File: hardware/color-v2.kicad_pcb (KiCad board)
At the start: 2 copper layers, 25 x 20 mm, 29 parts, among them P1 CON-SENSOR2, P2 DEBUG, P3 BOOT, Q1 2N7002P, U1 VEML6040, U2 XMC1XXX24, U3 DRILL, U4 DRILL, U5 DRILL, U6 DRILL

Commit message: fix drc error
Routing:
- net GND: track 24.8 -> 26.4 mm

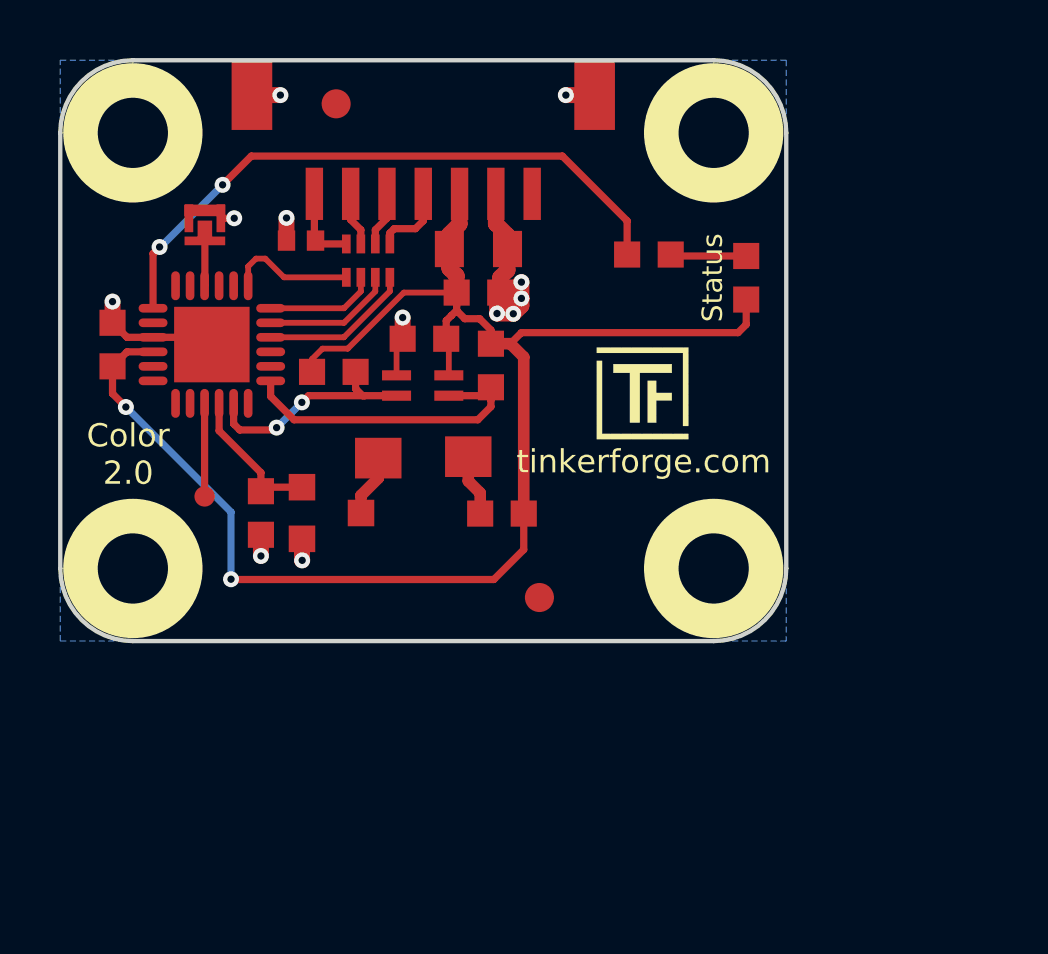
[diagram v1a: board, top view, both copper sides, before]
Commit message: changed colorsensor to TCS3472
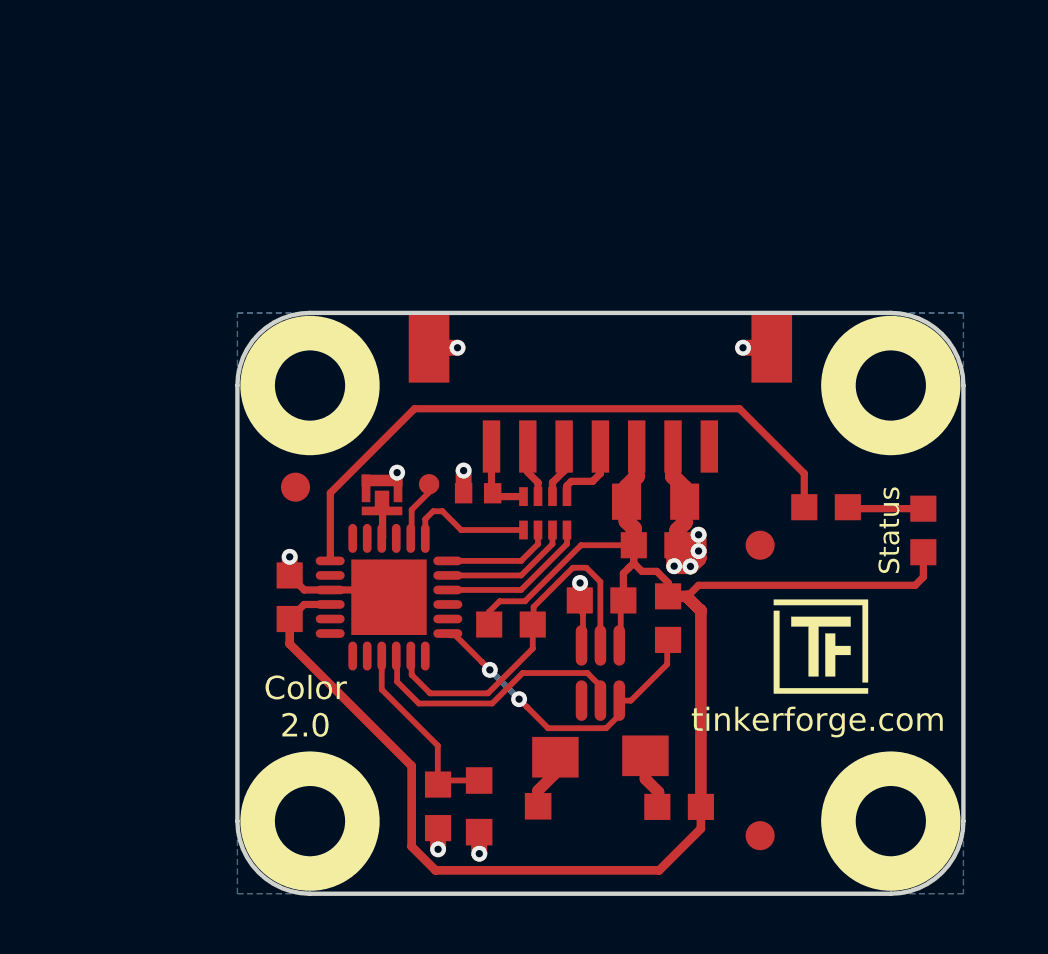
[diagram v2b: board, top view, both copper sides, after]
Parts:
- removed the Fiducial_Mark at (103.3, 62.7)
- removed the Fiducial_Mark at (110.3, 79.7)
- added Fiducial_Mark: VAL**, kicad-libraries:Fiducial_Mark, F.Cu at (117.9, 77.9)
- added Fiducial_Mark: VAL**, kicad-libraries:Fiducial_Mark, F.Cu at (117.9, 87.9)
- added Fiducial_Mark: VAL**, kicad-libraries:Fiducial_Mark, F.Cu at (101.9, 75.9)
- G***: value Logo_31x31 -> LOGO
- U1: value VEML6040 -> TCS3472; footprint kicad-libraries:OPLGA4 -> kicad-libraries:FN-TCS3472
- moved G*** 22.2 mm to (119.0, 80.0)
- moved G*** 12.9 mm to (120.0, 81.4)
- moved D1 12.0 mm to (112.4, 85.2)
- moved R1 11.8 mm to (106.8, 86.9)
- moved Q1 11.8 mm to (109.2, 86.9)
- moved R2 11.8 mm to (115.1, 86.9)
- moved U1 11.6 mm to (112.4, 82.3), turned to 270 degrees
- moved P3 11.1 mm to (104.9, 76.2)
- moved C1 10.9 mm to (112.4, 79.8)
- moved C5 10.6 mm to (101.7, 79.7)
- moved P1 10.6 mm to (112.4, 69.9)
- moved R4 10.6 mm to (114.7, 80.4)
- moved R5 10.6 mm to (120.2, 76.6)
- moved U2 10.6 mm to (105.1, 79.7)
- moved U3 10.6 mm to (102.4, 72.4)
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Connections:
- P1 pad 1: Net-(P1-Pad1) -> (no net)
- U1 pad 1: GND -> VCC
- U1 pad 3: SCL -> GND
- U1 pad 4: VCC -> (no net)
- U2 pad 11: Net-(U2-Pad11) -> (no net)
- U2 pad 12: Net-(U2-Pad12) -> (no net)
- U2 pad 13: Net-(U2-Pad13) -> (no net)
- U2 pad 14: Net-(U2-Pad14) -> (no net)
- U2 pad 15: Net-(P2-Pad1) -> LED
- U2 pad 16: LED -> INT
- U2 pad 18: Net-(U2-Pad18) -> (no net)
- U2 pad 2: Net-(U2-Pad2) -> Net-(P2-Pad1)
- U2 pad 20: Net-(U2-Pad20) -> (no net)
- U2 pad 21: Net-(U2-Pad21) -> (no net)
- U2 pad 3: Net-(U2-Pad3) -> (no net)
- U2 pad 5: Net-(U2-Pad5) -> (no net)
- U2 pad 6: Net-(U2-Pad6) -> (no net)
- U2 pad 8: Net-(U2-Pad8) -> (no net)
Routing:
- net INT: track 0.00 -> 9.43 mm
- net SDA: track 8.04 -> 12.5 mm, vias 2 -> 0
- net VCC: track 53.9 -> 57.5 mm, vias 2 -> 0
- net LED: track 5.09 -> 6.68 mm
- net Net-(P2-Pad1): track 3.20 -> 1.95 mm
- net Net-(R5-Pad1): track 21.7 -> 21.9 mm, vias 2 -> 0
- net SCL: track 11.3 -> 11.2 mm, vias 0 -> 2

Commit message: added fidutials
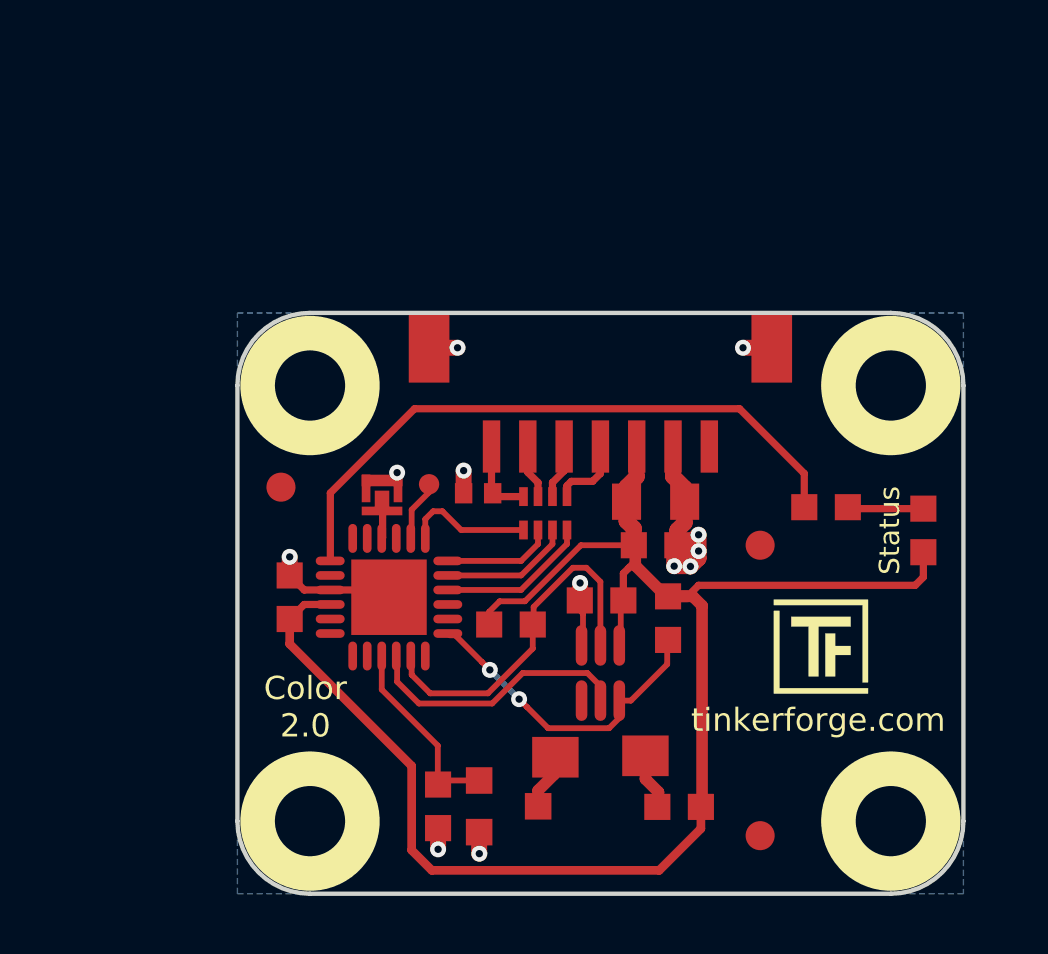
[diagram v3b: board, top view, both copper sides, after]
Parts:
- moved Fiducial_Mark 0.50 mm to (101.4, 75.9)
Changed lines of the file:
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@@
     (thickness 1.6)
     (drawings 12)
-    (tracks 197)
+    (tracks 193)
     (zones 0)
     (modules 30)
@@
   )
   (setup
-    (last_trace_width 0.25)
+    (last_trace_width 0.4)
     (user_trace_width 0.2)
     (user_trace_width 0.25)
@@
   )
   (module kicad-libraries:Fiducial_Mark (layer F.Cu)
-    (at 101.9 75.9)
+    (at 101.4 75.9)
     (attr smd)
     (fp_text reference Fiducial_Mark (at 0 0) (layer F.SilkS) hide
@@
   (segment (start 109.6 83.2) (end 108.593122 82.193122) (width 0.2) (layer B.Cu) (net 2))
   (segment (start 108.593122 82.193122) (end 108.593122 82.192407) (width 0.2) (layer B.Cu) (net 2))
-  (segment (start 113.05 83.25) (end 113.05 83.75) (width 0.2) (layer F.Cu) (net 2))
   (via (at 109.6 83.2) (size 0.55) (drill 0.25) (layers F.Cu B.Cu) (net 2))
-  (segment (start 110.6 84.2) (end 109.874999 83.474999) (width 0.2) (layer F.Cu) (net 2))
-  (segment (start 109.874999 83.474999) (end 109.6 83.2) (width 0.2) (layer F.Cu) (net 2))
-  (segment (start 113.05 83.75) (end 112.6 84.2) (width 0.2) (layer F.Cu) (net 2))
   (segment (start 107.400715 81) (end 108.318123 81.917408) (width 0.2) (layer F.Cu) (net 2))
   (via (at 108.593122 82.192407) (size 0.55) (drill 0.25) (layers F.Cu B.Cu) (net 2))
-  (segment (start 112.6 84.2) (end 110.6 84.2) (width 0.2) (layer F.Cu) (net 2))
   (segment (start 107.2 81) (end 107.400715 81) (width 0.2) (layer F.Cu) (net 2))
+  (segment (start 109.874999 83.474999) (end 109.6 83.2) (width 0.2) (layer F.Cu) (net 2))
+  (segment (start 110.6 84.2) (end 109.874999 83.474999) (width 0.2) (layer F.Cu) (net 2))
+  (segment (start 112.7 84.2) (end 110.6 84.2) (width 0.2) (layer F.Cu) (net 2))
+  (segment (start 113.05 83.25) (end 113.05 83.85) (width 0.2) (layer F.Cu) (net 2))
+  (segment (start 113.05 83.85) (end 112.7 84.2) (width 0.2) (layer F.Cu) (net 2))
   (segment (start 111.449998 78.67499) (end 110.1 80.024988) (width 0.2) (layer F.Cu) (net 3))
   (segment (start 111.917466 78.67499) (end 111.449998 78.67499) (width 0.2) (layer F.Cu) (net 3))
@@
   (segment (start 115.4 79.66) (end 114.73 79.66) (width 0.4) (layer F.Cu) (net 4))
   (segment (start 113.55 78.51) (end 113.55 78.52) (width 0.25) (layer F.Cu) (net 4))
-  (segment (start 114.73 79.19) (end 114.73 79.66) (width 0.25) (layer F.Cu) (net 4))
-  (segment (start 114.34 78.8) (end 114.73 79.19) (width 0.25) (layer F.Cu) (net 4))
-  (segment (start 113.83 78.8) (end 114.34 78.8) (width 0.25) (layer F.Cu) (net 4))
-  (segment (start 113.55 78.52) (end 113.83 78.8) (width 0.25) (layer F.Cu) (net 4))
   (segment (start 114.73 79.63) (end 114.73 79.66) (width 0.25) (layer F.Cu) (net 4))
   (segment (start 114.73 79.66) (end 114.73 79.37) (width 0.25) (layer F.Cu) (net 4))
@@
   (segment (start 113.1 79.58) (end 113.1 81.4) (width 0.2) (layer F.Cu) (net 4))
   (segment (start 113.19 79.49) (end 113.1 79.58) (width 0.2) (layer F.Cu) (net 4))
-  (segment (start 115.86 86.91) (end 115.86 80.16) (width 0.4) (layer F.Cu) (net 4))
-  (segment (start 115.5 79.8) (end 115.8 80.1) (width 0.4) (layer F.Cu) (net 4))
-  (segment (start 115.86 80.16) (end 115.5 79.8) (width 0.4) (layer F.Cu) (net 4))
+  (segment (start 115.86 87.66) (end 114.424999 89.095001) (width 0.3) (layer F.Cu) (net 4))
   (segment (start 101.7 81.3) (end 101.7 80.4) (width 0.3) (layer F.Cu) (net 4))
+  (segment (start 105.9 88.4) (end 105.9 85.5) (width 0.3) (layer F.Cu) (net 4))
   (segment (start 115.86 86.91) (end 115.86 87.66) (width 0.3) (layer F.Cu) (net 4))
-  (segment (start 114.424999 89.095001) (end 106.721815 89.095001) (width 0.3) (layer F.Cu) (net 4))
-  (segment (start 106.721815 89.095001) (end 105.9 88.273186) (width 0.3) (layer F.Cu) (net 4))
-  (segment (start 115.86 87.66) (end 114.424999 89.095001) (width 0.3) (layer F.Cu) (net 4))
-  (segment (start 105.9 88.273186) (end 105.9 85.5) (width 0.3) (layer F.Cu) (net 4))
+  (segment (start 106.595001 89.095001) (end 105.9 88.4) (width 0.3) (layer F.Cu) (net 4))
+  (segment (start 114.424999 89.095001) (end 106.595001 89.095001) (width 0.3) (layer F.Cu) (net 4))
   (segment (start 105.9 85.5) (end 101.7 81.3) (width 0.3) (layer F.Cu) (net 4))
-  (segment (start 115.4 79.7) (end 115.4 79.66) (width 0.4) (layer F.Cu) (net 4))
-  (segment (start 115.86 80.12) (end 115.82 80.12) (width 0.4) (layer F.Cu) (net 4))
-  (segment (start 115.82 80.12) (end 115.4 79.7) (width 0.4) (layer F.Cu) (net 4))
+  (segment (start 113.6 78.6) (end 113.6 77.9) (width 0.4) (layer F.Cu) (net 4))
+  (segment (start 114.73 79.66) (end 114.66 79.66) (width 0.4) (layer F.Cu) (net 4))
+  (segment (start 114.66 79.66) (end 113.6 78.6) (width 0.4) (layer F.Cu) (net 4))
+  (segment (start 115.58 79.66) (end 115.9 79.98) (width 0.4) (layer F.Cu) (net 4))
+  (segment (start 114.73 79.66) (end 115.58 79.66) (width 0.4) (layer F.Cu) (net 4))
+  (segment (start 115.9 79.98) (end 115.9 86.9) (width 0.4) (layer F.Cu) (net 4))
   (segment (start 113.95 85) (end 114.6 85) (width 0.254) (layer F.Cu) (net 5))
   (segment (start 114.4 86.4) (end 114.4 86.9) (width 0.4) (layer F.Cu) (net 5))

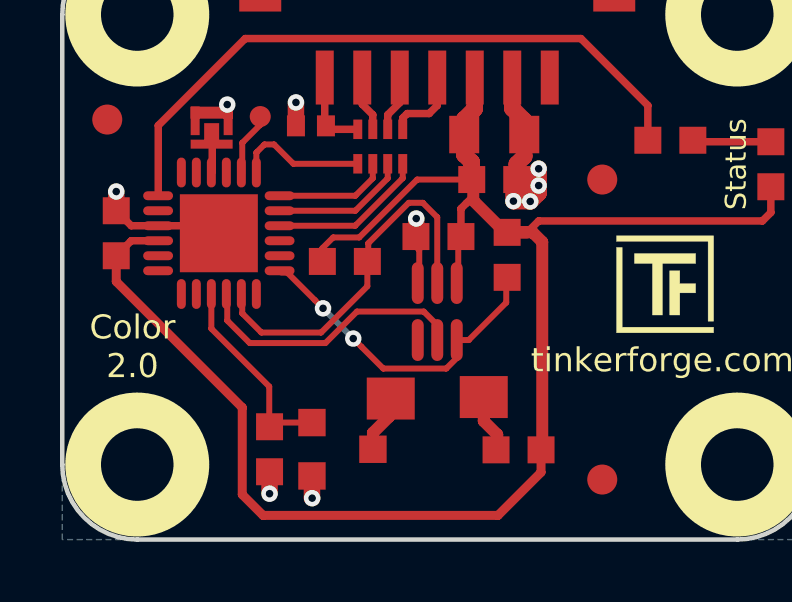
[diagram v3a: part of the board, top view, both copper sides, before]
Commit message: changed to XMC1300
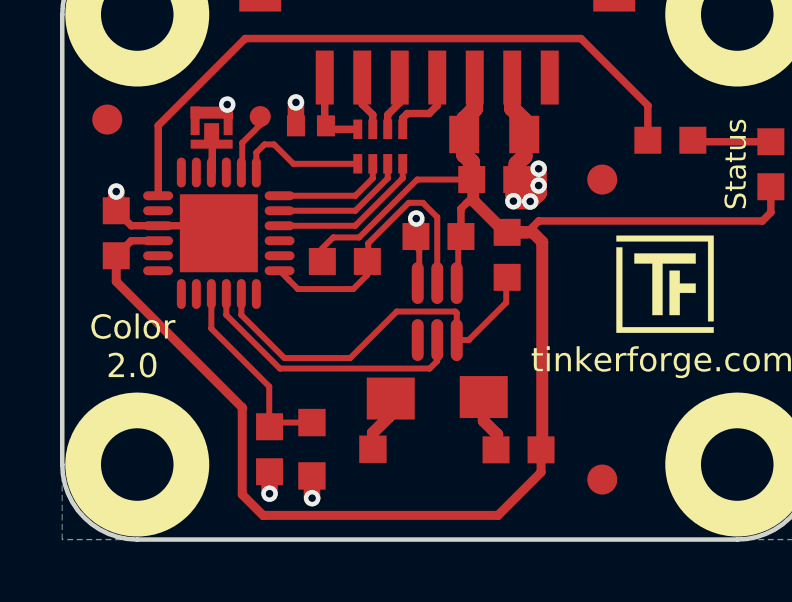
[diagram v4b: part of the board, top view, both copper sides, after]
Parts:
- U2: value XMC1XXX24 -> XMC1300
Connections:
- P1 pad 1: (no net) -> Net-(P1-Pad1)
- R3 pad 2: SDA -> SCL
- R4 pad 2: SCL -> SDA
- U1 pad 2: SDA -> SCL
- U1 pad 4: (no net) -> Net-(U1-Pad4)
- U1 pad 6: SCL -> SDA
- U2 pad 11: (no net) -> Net-(U2-Pad11)
- U2 pad 12: (no net) -> Net-(U2-Pad12)
- U2 pad 13: (no net) -> Net-(U2-Pad13)
- U2 pad 14: (no net) -> Net-(U2-Pad14)
- U2 pad 18: (no net) -> Net-(U2-Pad18)
- U2 pad 20: (no net) -> Net-(U2-Pad20)
- U2 pad 21: (no net) -> Net-(U2-Pad21)
- U2 pad 3: (no net) -> Net-(U2-Pad3)
- U2 pad 5: (no net) -> Net-(U2-Pad5)
- U2 pad 6: (no net) -> Net-(U2-Pad6)
- U2 pad 8: (no net) -> Net-(U2-Pad8)
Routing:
- net SCL: track 11.3 -> 9.75 mm, vias 2 -> 0
- net SDA: track 12.5 -> 14.0 mm
